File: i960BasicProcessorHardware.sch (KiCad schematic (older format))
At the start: 69 parts, among them J1 Conn_02x16_Odd_Even, J10 Conn_01x03, J11 Conn_01x08, J2 Conn_02x39_Odd_Even, J3 Conn_01x03, J4 Conn_02x05_Odd_Even, J5 Conn_02x05_Odd_Even, J6 Conn_02x05_Odd_Even, J7 Conn_01x06, J9 Conn_01x11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

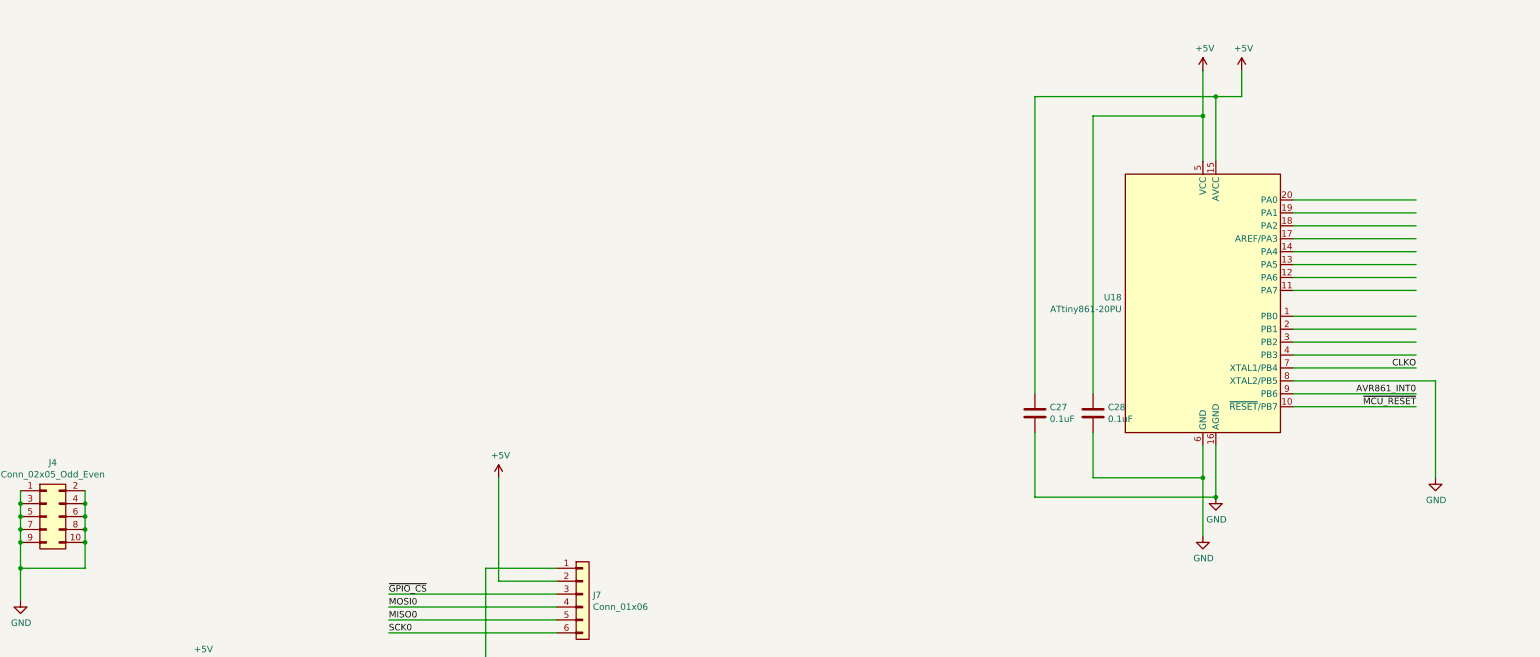
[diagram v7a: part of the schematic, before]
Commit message: Move the attiny861 schematic to a sub schematic
I am planning to have multiple of them
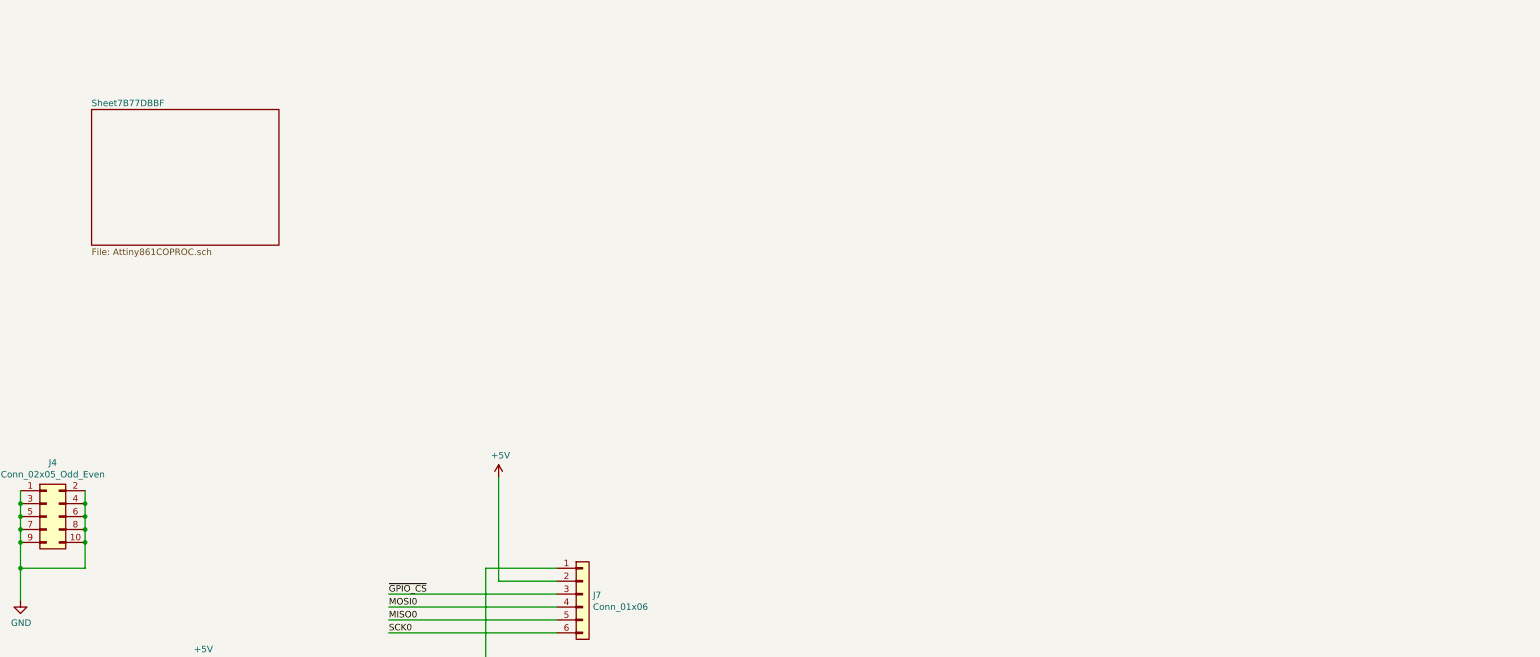
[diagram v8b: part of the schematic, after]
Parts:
- removed C27, C28: 0.1uF, Capacitor_SMD:C_0805_2012Metric_Pad1.18x1.45mm_HandSolder, symbol Device:C
- removed U18: ATtiny861-20PU, Package_DIP:DIP-20_W7.62mm, symbol MCU_Microchip_ATtiny:ATtiny861-20PU
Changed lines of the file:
@@
 $Descr A1 33110 23386
 encoding utf-8
-Sheet 1 1
+Sheet 1 2
 Title "i960Sx Basic Processor Hardware Board"
 Date "2021-10-16"
@@
 	1    0    0    -1
 $EndComp
-$Comp
-L MCU_Microchip_ATtiny:ATtiny861-20PU U18
-U 1 1 7A5F676E
-P 22700 2750
-F 0 "U18" H 22071 2796 50  0000 R CNN
-F 1 "ATtiny861-20PU" H 22071 2705 50  0000 R CNN
-F 2 "Package_DIP:DIP-20_W7.62mm" H 22700 2750 50  0001 C CIN
-F 3 "http://ww1.microchip.com/downloads/en/DeviceDoc/atmel-2588-8-bit-avr-microcontrollers-tinyavr-attiny261-attiny461-attiny861_datasheet.pdf" H 22700 2750 50  0001 C CNN
-	1    22700 2750
-	1    0    0    -1
-$EndComp
-Wire Wire Line
-	22700 1650 22700 1300
-Wire Wire Line
-	22700 1300 21850 1300
-Wire Wire Line
-	21850 1300 21850 3450
-Wire Wire Line
-	21850 4100 22700 4100
-Wire Wire Line
-	22700 4100 22700 3850
-$Comp
-L Device:C C28
-U 1 1 7A6C09AB
-P 21850 3600
-F 0 "C28" H 21965 3646 50  0000 L CNN
-F 1 "0.1uF" H 21965 3555 50  0000 L CNN
-F 2 "Capacitor_SMD:C_0805_2012Metric_Pad1.18x1.45mm_HandSolder" H 21888 3450 50  0001 C CNN
-F 3 "~" H 21850 3600 50  0001 C CNN
-	1    21850 3600
-	1    0    0    -1
-$EndComp
-Wire Wire Line
-	21850 3750 21850 4100
-$Comp
-L Device:C C27
-U 1 1 7A6C1395
-P 21400 3600
-F 0 "C27" H 21515 3646 50  0000 L CNN
-F 1 "0.1uF" H 21515 3555 50  0000 L CNN
-F 2 "Capacitor_SMD:C_0805_2012Metric_Pad1.18x1.45mm_HandSolder" H 21438 3450 50  0001 C CNN
-F 3 "~" H 21400 3600 50  0001 C CNN
-	1    21400 3600
-	1    0    0    -1
-$EndComp
-Wire Wire Line
-	21400 3450 21400 1150
-Wire Wire Line
-	21400 1150 22800 1150
-Wire Wire Line
-	22800 1150 22800 1650
-Wire Wire Line
-	22800 3850 22800 4250
-Wire Wire Line
-	22800 4250 21400 4250
-Wire Wire Line
-	21400 4250 21400 3750
-Wire Wire Line
-	22700 4100 22700 4550
-Connection ~ 22700 4100
-$Comp
-L power:GND #PWR0104
-U 1 1 7A91E3FB
-P 22700 4550
-F 0 "#PWR0104" H 22700 4300 50  0001 C CNN
-F 1 "GND" H 22705 4377 50  0000 C CNN
-F 2 "" H 22700 4550 50  0001 C CNN
-F 3 "" H 22700 4550 50  0001 C CNN
-	1    22700 4550
-	1    0    0    -1
-$EndComp
-$Comp
-L power:GND #PWR0105
-U 1 1 7A91E440
-P 22800 4250
-F 0 "#PWR0105" H 22800 4000 50  0001 C CNN
-F 1 "GND" H 22805 4077 50  0000 C CNN
-F 2 "" H 22800 4250 50  0001 C CNN
-F 3 "" H 22800 4250 50  0001 C CNN
-	1    22800 4250
-	1    0    0    -1
-$EndComp
-Connection ~ 22800 4250
-Wire Wire Line
-	22700 1300 22700 950
-Connection ~ 22700 1300
-Wire Wire Line
-	22800 1150 23000 1150
-Wire Wire Line
-	23000 1150 23000 950
-Connection ~ 22800 1150
-$Comp
-L power:+5V #PWR?
-U 1 1 7AAB2892
-P 22700 950
-AR Path="/640CD6D6/7AAB2892" Ref="#PWR?"  Part="1"
-AR Path="/7AAB2892" Ref="#PWR0106"  Part="1"
-F 0 "#PWR0106" H 22700 800 50  0001 C CNN
-F 1 "+5V" H 22715 1123 50  0000 C CNN
-F 2 "" H 22700 950 50  0001 C CNN
-F 3 "" H 22700 950 50  0001 C CNN
-	1    22700 950
-	1    0    0    -1
-$EndComp
-$Comp
-L power:+5V #PWR?
-U 1 1 7AAB2CAF
-P 23000 950
-AR Path="/640CD6D6/7AAB2CAF" Ref="#PWR?"  Part="1"
-AR Path="/7AAB2CAF" Ref="#PWR0107"  Part="1"
-F 0 "#PWR0107" H 23000 800 50  0001 C CNN
-F 1 "+5V" H 23015 1123 50  0000 C CNN
-F 2 "" H 23000 950 50  0001 C CNN
-F 3 "" H 23000 950 50  0001 C CNN
-	1    23000 950
-	1    0    0    -1
-$EndComp
-Wire Wire Line
-	23400 1950 24350 1950
-Wire Wire Line
-	23400 2050 24350 2050
-Wire Wire Line
-	23400 2150 24350 2150
-Wire Wire Line
-	23400 2250 24350 2250
-Wire Wire Line
-	23400 2350 24350 2350
-Wire Wire Line
-	23400 2450 24350 2450
-Wire Wire Line
-	23400 2550 24350 2550
-Wire Wire Line
-	23400 2650 24350 2650
-Wire Wire Line
-	23400 2850 24350 2850
-Wire Wire Line
-	23400 2950 24350 2950
-Wire Wire Line
-	23400 3050 24350 3050
-Wire Wire Line
-	23400 3150 24350 3150
-Wire Wire Line
-	23400 3250 24350 3250
-Wire Wire Line
-	23400 3450 24350 3450
-Wire Wire Line
-	23400 3550 24350 3550
-Text Label 24350 3550 2    50   ~ 0
-~MCU_RESET
-Text Label 24350 3250 2    50   ~ 0
-CLKO
-Wire Wire Line
-	24500 3350 24500 4100
-Wire Wire Line
-	23400 3350 24500 3350
-$Comp
-L power:GND #PWR0108
-U 1 1 7B4FE180
-P 24500 4100
-F 0 "#PWR0108" H 24500 3850 50  0001 C CNN
-F 1 "GND" H 24505 3927 50  0000 C CNN
-F 2 "" H 24500 4100 50  0001 C CNN
-F 3 "" H 24500 4100 50  0001 C CNN
-	1    24500 4100
-	1    0    0    -1
-$EndComp
-Text Label 24350 3450 2    50   ~ 0
-AVR861_INT0
+$Sheet
+S 14100 1250 1450 1050
+U 7B77DBC0
+F0 "Sheet7B77DBBF" 50
+F1 "Attiny861COPROC.sch" 50
+$EndSheet
 $EndSCHEMATC
